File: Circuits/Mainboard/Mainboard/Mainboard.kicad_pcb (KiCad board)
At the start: 2 copper layers, 170.1 x 170.1 mm, 71 parts, among them IC1 LM74500QDDFRQ1, IC2 LM74500QDDFRQ1, IC3 2536030320001, IC4 SX1280IMLTRT, IC5 SKY66122-11, IC6 TS2596CM533_RNG, IC7 TPS563300DRLR, J1 XT60PW-M, J10 B5P-VH_LF__SN_, J11 B6B-PH-K-S, J12 B5P-VH_LF__SN_, J13 B6B-PH-K-S, J14 B5P-VH_LF__SN_, J15 SMA-J-P-H-RA-TH1, J16 B5P-VH_LF__SN_, J2 XT60PW-M, J22 Conn_01x04_Pin, J23 Conn_01x04_Pin, J25 Conn_01x06_Pin, J26 Conn_01x04_Pin, J27 Conn_01x04_Pin, J3 Conn_01x06_Pin, J5 B6B-PH-K-S, J6 B5P-VH_LF__SN_, J7 B6B-PH-K-S, J8 Conn_01x06_Pin, J9 Conn_01x04_Pin, Q1 PSMN6R7-40MLDX, Q2 PSMN6R7-40MLDX, U1 NUCLEOH723ZG

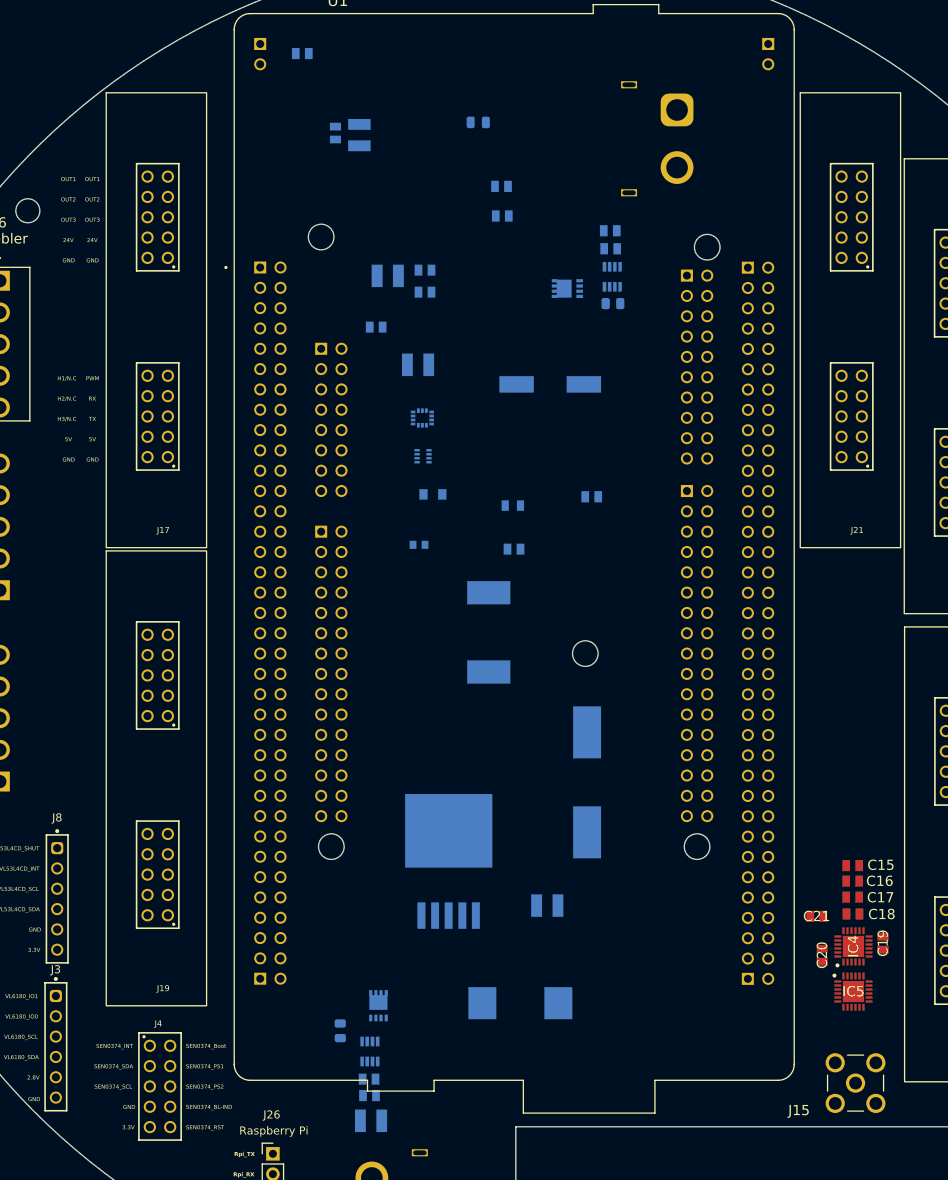
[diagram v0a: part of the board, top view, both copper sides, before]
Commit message: Removed components from the pcb to make it easier to work with
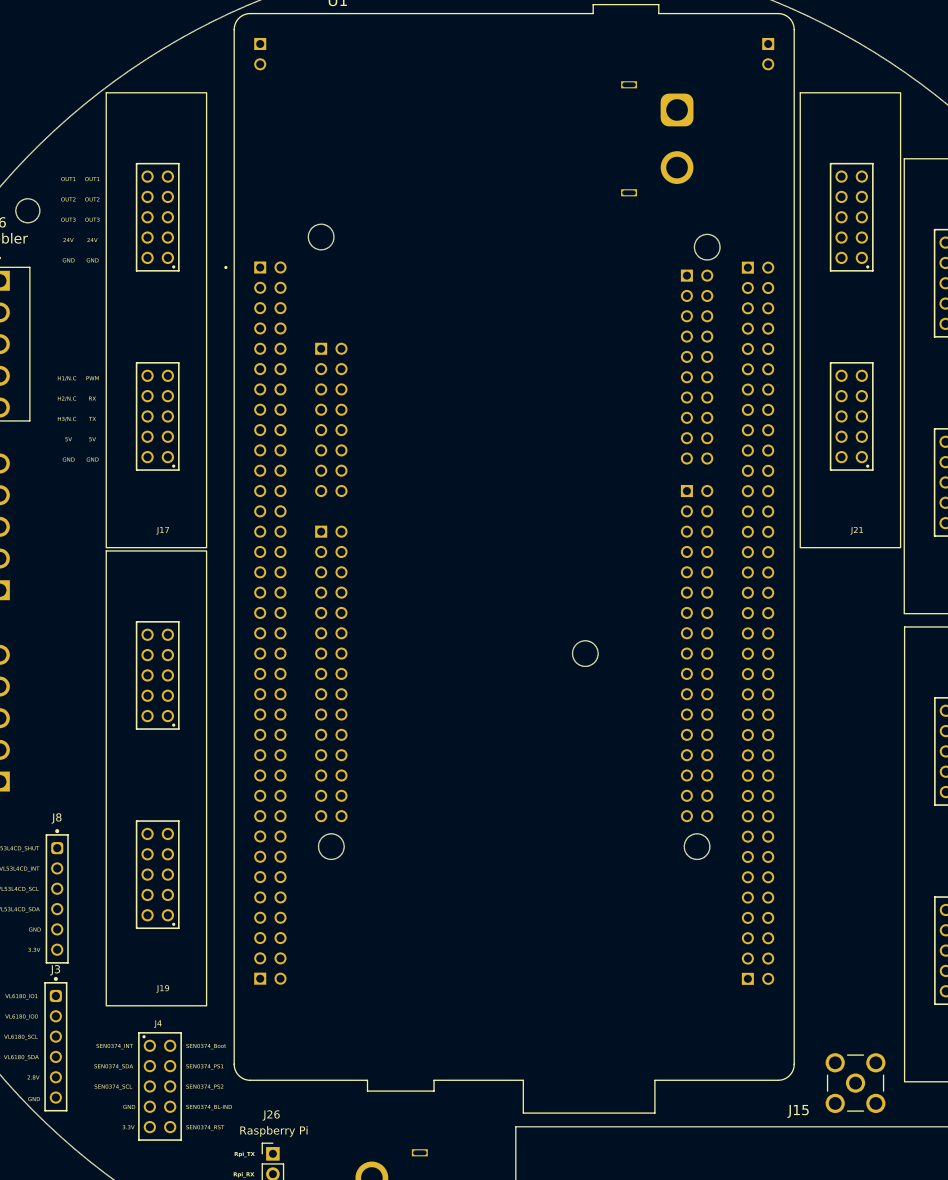
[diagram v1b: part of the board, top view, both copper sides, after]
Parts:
- removed C1, C12, C13, C14, C2, C23, C25, C26, C27, C3, C4, C6, C7: 0.1uF, 885012007063:CAPC2012X90N
- removed C10, C11, C24, C8, C9: 10uF, 885012209073:CAPC3225X280N
- removed C15, C17: 100nF, 885012007063:CAPC2012X90N
- removed C16, C18: 1nF, 885012007063:CAPC2012X90N
- removed C19: 1uF, 885012007063:CAPC2012X90N
- removed C20, C21: 10nF, 885012007063:CAPC2012X90N
- removed C22: 470uF, Altium_WCAP-ASLL (rev24b):WCAP-ASLL_D16H17
- removed C28: 47uF, Altium_WCAP-CSGP (rev24b):WCAP-CSGP_0805_L2W1.25H1.25
- removed C5: 220uF, 865080657018:CAPAE1030X1050N
- removed C8: 0.1uF, Capacitor_SMD:C_0805_2012Metric
- removed IC1, IC2: LM74500QDDFRQ1, LM74500QDDFRQ1:SOT65P280X110-8N
- removed IC3: 2536030320001, WSEN-ISDS:2536030320001
- removed IC4: SX1280IMLTRT, SX1280IMLTRT:QFN50P400X400X100-25N-D
- removed IC5: SKY66122-11, SKY66122-11:QFN50P400X400X100-25N-D
- removed IC6: TS2596CM533_RNG, TS2596CM533_RNG:TS2596CM550RNG
- removed IC7: TPS563300DRLR, TPS563300DRLR:TPS62932DRLR
- removed L1: 8.2uH, WE-HCC (rev24a):WE-HCC_1210
- removed L2: AMRM00101040470MA1, AMRM00101040470MA1:AMRM00101040470MA1
- removed Q1, Q2: PSMN6R7-40MLDX, PSMN6R740MLDX:PSMN6R740MLDX
- removed R1, R2: 10, Resistor_SMD:R_0805_2012Metric
- removed R3: 52.3kOhm, CRCW060352K3FKEA:RESC1608X50N
- removed R4: 10kOhm, Altium_WRIS-RSKS (rev23a):WRIS-RSKS_0805_Wave

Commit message: STP to pointer
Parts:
- added C1: 0.1uF, 885012007063:CAPC2012X90N, F.Cu at (62.9, 80.8)
- added C10: 0.1uF, 885012007063:CAPC2012X90N, F.Cu at (64.7, 49.6)
- added C10: 10uF, 885012209073:CAPC3225X280N, F.Cu at (49.6, 109.8)
- added C11: 10uF, 885012209073:CAPC3225X280N, F.Cu at (49.6, 114.0)
- added C12: 0.1uF, 885012007063:CAPC2012X90N, F.Cu at (66.8, 83.6)
- added C13: 10uF, 885012209073:CAPC3225X280N, F.Cu at (79.5, 41.4)
- added C14: 0.1uF, 885012007063:CAPC2012X90N, F.Cu at (66.8, 86.3)
- added C15: 100nF, 885012007063:CAPC2012X90N, F.Cu at (66.8, 89.1)
- added C16: 1nF, 885012007063:CAPC2012X90N, F.Cu at (66.8, 91.8)
- added C17: 100nF, 885012007063:CAPC2012X90N, F.Cu at (70.7, 80.8)
- added C18: 1nF, 885012007063:CAPC2012X90N, F.Cu at (70.7, 83.6)
- added C19: 1uF, 885012007063:CAPC2012X90N, F.Cu at (70.7, 86.3)
- added C2: 0.1uF, 885012007063:CAPC2012X90N, F.Cu at (62.9, 83.6)
- added C20: 10nF, 885012007063:CAPC2012X90N, F.Cu at (70.7, 89.1)
- added C21: 10nF, 885012007063:CAPC2012X90N, F.Cu at (70.7, 91.8)
- added C22: 470uF, Altium_WCAP-ASLL (rev24b):WCAP-ASLL_D16H17, F.Cu at (56.9, 70.2)
- added C22: 0.1uF, 885012007063:CAPC2012X90N, F.Cu at (64.7, 52.3)
- added C23: 47uF, Altium_WCAP-CSGP (rev24b):WCAP-CSGP_0805_L2W1.25H1.25, F.Cu at (78.2, 49.4)
- added C23: 0.1uF, 885012007063:CAPC2012X90N, F.Cu at (74.7, 80.8)
- added C24: 10uF, 885012209073:CAPC3225X280N, F.Cu at (49.6, 118.2)
- added C25: 0.1uF, 885012007063:CAPC2012X90N, F.Cu at (74.7, 83.6)
- added C26: 0.1uF, 885012007063:CAPC2012X90N, F.Cu at (74.7, 86.3)
- added C27: 0.1uF, 885012007063:CAPC2012X90N, F.Cu at (74.7, 89.1)
- added C28: 47uF, Altium_WCAP-CSGP (rev24b):WCAP-CSGP_0805_L2W1.25H1.25, F.Cu at (92.5, 71.1)
- added C29: 100nF, 885012007063:CAPC2012X90N, F.Cu at (74.7, 91.8)
- added C3: 0.1uF, 885012007063:CAPC2012X90N, F.Cu at (62.9, 86.3)
- added C30: 1nF, 885012007063:CAPC2012X90N, F.Cu at (78.6, 80.8)
- added C31: 100nF, 885012007063:CAPC2012X90N, F.Cu at (78.6, 83.6)
- added C32: 1nF, 885012007063:CAPC2012X90N, F.Cu at (78.6, 86.3)
- added C33: 100nF, 885012007063:CAPC2012X90N, F.Cu at (78.6, 89.1)
- added C34: 1nF, 885012007063:CAPC2012X90N, F.Cu at (78.6, 91.8)
- added C35: 0p8, Capacitor_SMD:C_0603_1608Metric, F.Cu at (54.3, 100.7)
- added C36: 1p5, Capacitor_SMD:C_0603_1608Metric, F.Cu at (54.3, 103.2)
- added C37: NA, Capacitor_SMD:C_0603_1608Metric, F.Cu at (54.3, 105.7)
- added C38: 0p5, Capacitor_SMD:C_0603_1608Metric, F.Cu at (54.3, 108.2)
- added C39: 100p, Capacitor_SMD:C_0603_1608Metric, F.Cu at (54.3, 110.7)
- added C4: 0.1uF, 885012007063:CAPC2012X90N, F.Cu at (62.9, 89.1)
- added C40: 47p, Capacitor_SMD:C_0603_1608Metric, F.Cu at (54.3, 113.2)
- added C41: 0p6, Capacitor_SMD:C_0603_1608Metric, F.Cu at (54.3, 115.7)
- added C42: NA, Capacitor_SMD:C_0603_1608Metric, F.Cu at (54.3, 118.2)
- added C43: 4.7uF, 885012209073:CAPC3225X280N, F.Cu at (79.5, 45.5)
- added C44: 0.1uF, 885012007063:CAPC2012X90N, F.Cu at (64.7, 55.1)
- added C5: 220uF, 865080657018:CAPAE1030X1050N, F.Cu at (84.4, 99.5)
- added C6: 0.1uF, 885012007063:CAPC2012X90N, F.Cu at (62.9, 91.8)
- added C7: 0.1uF, 885012007063:CAPC2012X90N, F.Cu at (66.8, 80.8)
- added C7: 10uF, 885012209073:CAPC3225X280N, F.Cu at (79.5, 37.2)
- added C8: 10uF, 885012209073:CAPC3225X280N, F.Cu at (49.6, 101.5)
- added C9: 10uF, 885012209073:CAPC3225X280N, F.Cu at (49.6, 105.7)
- added IC1: LM74500QDDFRQ1, LM74500QDDFRQ1:SOT65P280X110-8N, F.Cu at (93.2, 63.2)
- added IC2: LM74500QDDFRQ1, LM74500QDDFRQ1:SOT65P280X110-8N, F.Cu at (93.2, 67.7)
- added IC3: 2536030320001, WSEN-ISDS:2536030320001, F.Cu at (83.6, 89.2)
- added IC4: SX1280IMLTRT, SX1280IMLTRT:QFN50P400X400X100-25N-D, F.Cu at (94.0, 108.9)
- added IC5: SKY66122-11, SKY66122-11:QFN50P400X400X100-25N-D, F.Cu at (94.0, 115.2)
- added IC6: TS2596CM533_RNG, TS2596CM533_RNG:TS2596CM550RNG, F.Cu at (53.9, 90.9)
- added IC6: TPS563300DRLR, TPS563300DRLR:TPS62932DRLR, F.Cu at (69.3, 50.8)
- added IC7: TPS563300DRLR, TPS563300DRLR:TPS62932DRLR, F.Cu at (89.3, 89.0)
- added L1: 8.2uH, WE-HCC (rev24a):WE-HCC_1210, F.Cu at (83.9, 112.2)
- added L2: AMRM00101040470MA1, AMRM00101040470MA1:AMRM00101040470MA1, F.Cu at (69.0, 100.5)
- added L2: 5.6uH, Power Inductors - SMD WE-PD 5.6uH 6A:7447714220, F.Cu at (69.8, 41.7)
- added P1: 66200621122, WR-MPC3 3.00 mm Male Header Dual Row Vertical:66200621122, F.Cu at (158.6, 61.8)
- added Q1: PSMN6R7-40MLDX, PSMN6R740MLDX:PSMN6R740MLDX, F.Cu at (83.8, 82.8)
- added Q2: PSMN6R7-40MLDX, PSMN6R740MLDX:PSMN6R740MLDX, F.Cu at (90.2, 82.8)
- added R1: 10, Resistor_SMD:R_0805_2012Metric, F.Cu at (58.5, 100.9)
- added R2: 10, Resistor_SMD:R_0805_2012Metric, F.Cu at (58.5, 103.8)
- added R3: 52.3kOhm, CRCW060352K3FKEA:RESC1608X50N, F.Cu at (93.8, 90.0)
- added R4: 10kOhm, Altium_WRIS-RSKS (rev23a):WRIS-RSKS_0805_Wave, F.Cu at (94.1, 87.6)
- added R5: 3n, Resistor_SMD:R_0805_2012Metric, F.Cu at (58.5, 106.8)
- added R6: 2n7, Resistor_SMD:R_0805_2012Metric, F.Cu at (58.5, 109.7)
- added R7: 3n9, Resistor_SMD:R_0805_2012Metric, F.Cu at (58.5, 112.7)
- added R8: 30.9kOhm, Resistor_SMD:R_0805_2012Metric, F.Cu at (68.8, 54.9)
- added R9: 10kOhm, Altium_WRIS-RSKS (rev23a):WRIS-RSKS_0805_Wave, F.Cu at (74.1, 49.4)
- added U2: ADP121-AUJZ28R7, ADP121-AUJZ28R7:UJ-5_ADI, F.Cu at (109.0, 58.7)
- J17: value ~ -> Conn_01x04_Pin; footprint 61301021821:ESC_Adapter_socket -> Connector_PinHeader_2.54mm:PinHeader_1x04_P2.54mm_Vertical; moved to B.Cu
- J18, J19, J20, J21: footprint 61301021821:ESC_Adapter_socket -> B-G431B-ESC1:ESC_Adapter_socket
- J22: value Conn_01x04_Pin -> ~; footprint Connector_PinHeader_2.54mm:PinHeader_1x04_P2.54mm_Vertical -> B-G431B-ESC1:ESC_Adapter_socket; moved to F.Cu
- moved J1 120.1 mm to (191.1, 182.5), turned to 0 degrees
- moved J4 105.3 mm to (244.8, 162.3)
- moved J26 101.0 mm to (241.9, 140.6)
- moved J18 41.3 mm to (227.7, 78.1)
- moved J22 37.8 mm to (141.6, 78.5), turned to 0 degrees
- moved J20 36.9 mm to (227.7, 141.2)
- moved J17 31.3 mm to (111.3, 101.4), turned to 180 degrees
- moved J21 26.9 mm to (240.2, 84.6)
- moved J19 24.6 mm to (141.6, 141.4)
- moved J2 22.3 mm to (172.0, 182.1), turned to 0 degrees
- moved U1 19.1 mm to (185.0, 137.1)
- moved J15 14.4 mm to (239.9, 175.8)
- moved J23 0.31 mm to (111.3, 148.1)
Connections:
- J11 pad 2: /5V -> 5V
- J13 pad 2: /5V -> 5V
- J15 pad 1: unconnected-(J15-Pad1) -> Net-(C42-Pad2)
- J15 pad 2: unconnected-(J15-Pad2) -> GND
- J15 pad 3: unconnected-(J15-Pad3) -> GND
- J15 pad 4: unconnected-(J15-Pad4) -> GND
- J15 pad 5: unconnected-(J15-Pad5) -> GND
- J17 pad 1: GND -> 5V
- J17 pad 2: GND -> /M1_Encoder_A
- J17 pad 3: /5V -> /M1_Encoder_B
- J17 pad 4: /5V -> GND
- J18 pad 1: GND -> /M2_OUT1
- J18 pad 10: /M2_H1 -> /M2_OUT3
- J18 pad 11: GND -> /M2_OUT3
- J18 pad 12: GND -> /M2_OUT3
- J18 pad 15: /M2_OUT3 -> 24V
- J18 pad 16: /M2_OUT3 -> 24V
- J18 pad 17: /M2_OUT2 -> GND
- J18 pad 18: /M2_OUT2 -> GND
- J18 pad 19: /M2_OUT1 -> GND
- J18 pad 2: GND -> /M2_OUT1
- J18 pad 20: /M2_OUT1 -> GND
- J18 pad 3: /5V -> /M2_OUT1
- J18 pad 4: /5V -> /M2_OUT1
- J18 pad 5: /M2_TX -> /M2_OUT2
- J18 pad 6: /M2_H3 -> /M2_OUT2
- J18 pad 7: /M2_RX -> /M2_OUT2
- J18 pad 8: /M2_H2 -> /M2_OUT2
- J18 pad 9: /M2_PWM -> /M2_OUT3
- J19 pad 1: GND -> /M3_OUT1
- J19 pad 10: /M3_H1 -> /M3_OUT3
- J19 pad 11: GND -> /M3_OUT3
- J19 pad 12: GND -> /M3_OUT3
- J19 pad 15: /M3_OUT3 -> 24V
- J19 pad 16: /M3_OUT3 -> 24V
- J19 pad 17: /M3_OUT2 -> GND
- J19 pad 18: /M3_OUT2 -> GND
- J19 pad 19: /M3_OUT1 -> GND
- J19 pad 2: GND -> /M3_OUT1
- J19 pad 20: /M3_OUT1 -> GND
- J19 pad 3: /5V -> /M3_OUT1
- J19 pad 4: /5V -> /M3_OUT1
- J19 pad 5: /M3_TX -> /M3_OUT2
- J19 pad 6: /M3_H3 -> /M3_OUT2
- J19 pad 7: /M3_RX -> /M3_OUT2
- J19 pad 8: /M3_H2 -> /M3_OUT2
- J19 pad 9: /M3_PWM -> /M3_OUT3
- J20 pad 1: GND -> /M4_OUT1
- J20 pad 10: /M4_H1 -> /M4_OUT3
- J20 pad 11: GND -> /M4_OUT3
- J20 pad 12: GND -> /M4_OUT3
- J20 pad 15: /M4_OUT3 -> 24V
- J20 pad 16: /M4_OUT3 -> 24V
- J20 pad 17: /M4_OUT2 -> GND
- J20 pad 18: /M4_OUT2 -> GND
- J20 pad 19: /M4_OUT1 -> GND
- J20 pad 2: GND -> /M4_OUT1
- J20 pad 20: /M4_OUT1 -> GND
- J20 pad 3: /5V -> /M4_OUT1
- J20 pad 4: /5V -> /M4_OUT1
- J20 pad 5: /M4_TX -> /M4_OUT2
- J20 pad 6: /M4_H3 -> /M4_OUT2
- J20 pad 7: /M4_RX -> /M4_OUT2
- J20 pad 8: /M4_H2 -> /M4_OUT2
- J20 pad 9: /M4_PWM -> /M4_OUT3
- J21 pad 1: GND -> /M5_OUT1
- J21 pad 10: unconnected-(J21-L10-Pad10) -> /M5_OUT3
- J21 pad 11: GND -> /M5_OUT3
- J21 pad 12: GND -> /M5_OUT3
- J21 pad 15: /M5_OUT3 -> 24V
- J21 pad 16: /M5_OUT3 -> 24V
- J21 pad 17: /M5_OUT2 -> GND
- J21 pad 18: /M5_OUT2 -> GND
- J21 pad 19: /M5_OUT1 -> GND
- J21 pad 2: GND -> /M5_OUT1
- J21 pad 20: /M5_OUT1 -> GND
- J21 pad 3: /5V -> /M5_OUT1
- J21 pad 4: /5V -> /M5_OUT1
- J21 pad 5: /M5_TX -> /M5_OUT2
- J21 pad 6: unconnected-(J21-L6-Pad6) -> /M5_OUT2
- J21 pad 7: /M5_RX -> /M5_OUT2
- J21 pad 8: unconnected-(J21-L8-Pad8) -> /M5_OUT2
- J21 pad 9: /M5_PWM -> /M5_OUT3
- J22 pad 1: /5V -> /M1_OUT1
- J22 pad 2: /M1_Encoder_A -> /M1_OUT1
- J22 pad 3: /M1_Encoder_B -> /M1_OUT1
- J22 pad 4: GND -> /M1_OUT1
- J23 pad 1: /5V -> 5V
- J26 pad 3: /5V -> 5V
- J27 pad 1: /5V -> 5V
- J3 pad 5: /2.8V -> 2.8V
- J5 pad 2: /5V -> 5V
- J5 pad 3: /M1_H3 -> /M1_H1
- J7 pad 2: /5V -> 5V
- J9 pad 1: /5V -> 5V
- U1 pad CN11_16: Net-(U1A-3V3) -> 3.3V
- U1 pad CN11_35: unconnected-(U1A-PC2-PadCN11_35) -> RF_MISO
- U1 pad CN11_37: unconnected-(U1A-PC3-PadCN11_37) -> RF_MOSI
- U1 pad CN11_42: unconnected-(U1A-PG2-PadCN11_42) -> /SEN0374_PS2
- U1 pad CN11_44: unconnected-(U1A-PG3-PadCN11_44) -> /SEN0374_BL-IND
- U1 pad CN11_52: unconnected-(U1A-PF2-PadCN11_52) -> /VL53L4CD_SHUT
- U1 pad CN12_2: unconnected-(U1B-PC8-PadCN12_2) -> /VL6180_IO0
- U1 pad CN12_25: unconnected-(U1B-PB10-PadCN12_25) -> RF_SCK
- U1 pad CN12_41: unconnected-(U1B-PD13-PadCN12_41) -> /SEN0374_INT
- U1 pad CN12_46: unconnected-(U1B-PD14-PadCN12_46) -> /SEN0374_Boot
- U1 pad CN12_48: unconnected-(U1B-PD15-PadCN12_48) -> /SEN0374_PS1
- U1 pad CN12_53: unconnected-(U1B-PE15-PadCN12_53) -> RF_CS
- U1 pad CN12_58: unconnected-(U1B-PF3-PadCN12_58) -> /VL53L4CD_INT
- U1 pad CN12_66: unconnected-(U1B-PG8-PadCN12_66) -> /VL6180_IO1
- U1 pad CN12_68: unconnected-(U1B-PG5-PadCN12_68) -> /ADPS-9960_VL
- U1 pad CN12_69: unconnected-(U1B-PG4-PadCN12_69) -> /SEN0374_RST
- U1 pad CN12_70: unconnected-(U1B-PG6-PadCN12_70) -> /ADPS-9960_INT
- U1 pad CN8_12: GND -> unconnected-(U1C-D48/SDMMC_CMD-PadCN8_12)
- U1 pad CN8_14: GND -> unconnected-(U1C-D49/IO-PadCN8_14)
- U1 pad CN8_8: 3.3V -> unconnected-(U1C-D46/SDMMC_D3-PadCN8_8)
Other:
- board size 170.1 x 170.1 mm -> 170 x 170 mm
- board text added: "RX/N.C"
- board text removed: "RX"

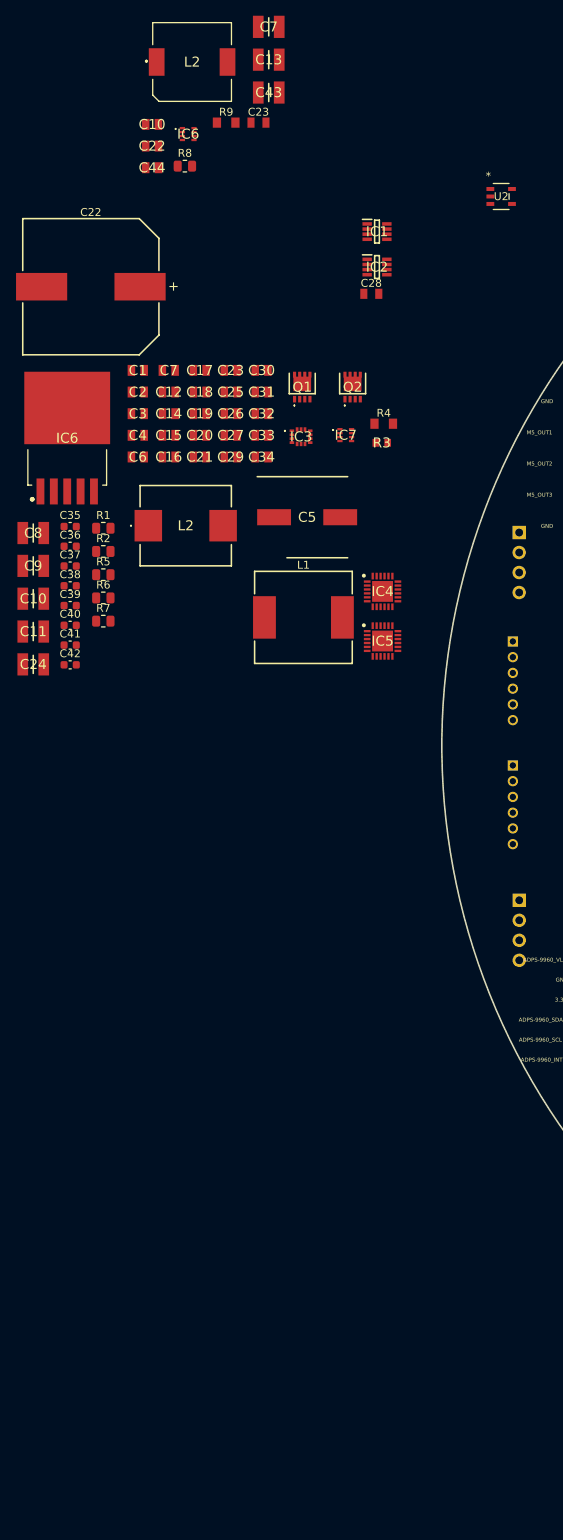
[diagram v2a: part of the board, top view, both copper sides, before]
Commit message: Added updated pin configuration to stm32
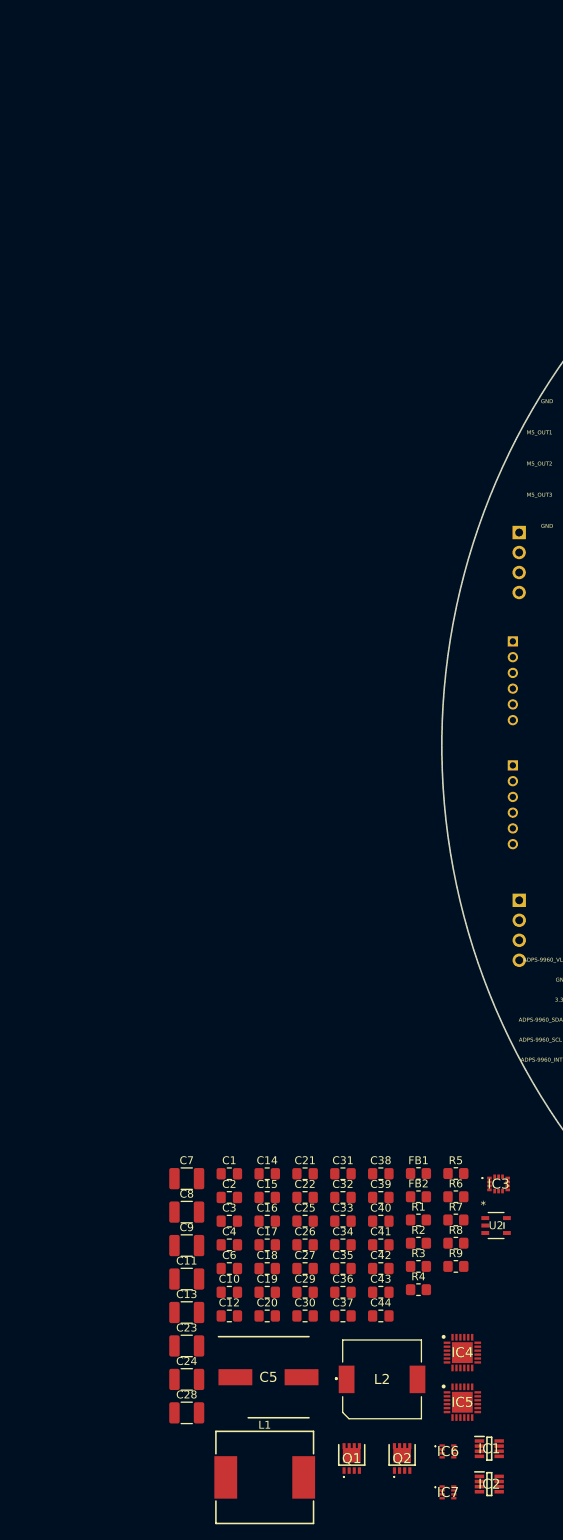
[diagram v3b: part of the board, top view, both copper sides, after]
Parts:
- removed the C10 at (64.7, 49.6)
- removed the C10 at (49.6, 109.8)
- removed the C22 at (56.9, 70.2)
- removed the C22 at (64.7, 52.3)
- removed the C23 at (78.2, 49.4)
- removed the C23 at (74.7, 80.8)
- removed the C7 at (66.8, 80.8)
- removed the C7 at (79.5, 37.2)
- removed the IC6 at (53.9, 90.9)
- removed the IC6 at (69.3, 50.8)
- removed the L2 at (69.0, 100.5)
- removed the L2 at (69.8, 41.7)
- added C10: 0.1uF, Capacitor_SMD:C_0805_2012Metric_Pad1.18x1.45mm_HandSolder, F.Cu at (74.5, 197.9)
- added C22: 0.1uF, Capacitor_SMD:C_0805_2012Metric_Pad1.18x1.45mm_HandSolder, F.Cu at (84.1, 185.9)
- added C23: 47uF, Capacitor_SMD:C_1210_3225Metric_Pad1.33x2.70mm_HandSolder, F.Cu at (69.1, 204.7)
- added C7: 10uF, Capacitor_SMD:C_1210_3225Metric_Pad1.33x2.70mm_HandSolder, F.Cu at (69.1, 183.5)
- added FB1: 120R, Resistor_SMD:R_0805_2012Metric_Pad1.20x1.40mm_HandSolder, F.Cu at (98.5, 182.8)
- added FB2: 120R, Resistor_SMD:R_0805_2012Metric_Pad1.20x1.40mm_HandSolder, F.Cu at (98.5, 185.8)
- added IC6: TPS563300DRLR, TPS563300DRLR:TPS62932DRLR, F.Cu at (102.3, 218.1)
- added L2: 5.6uH, Power Inductors - SMD WE-PD 5.6uH 6A:7447714220, F.Cu at (93.9, 209.0)
- C1, C12, C14, C15, C16, C17, C18, C19, C2, C20, C21, C25, C26, C27, C29, C3, C30, C31, C32, C33, C34, C4, C44, C6: footprint 885012007063:CAPC2012X90N -> Capacitor_SMD:C_0805_2012Metric_Pad1.18x1.45mm_HandSolder
- C11, C13, C24, C8, C9: footprint 885012209073:CAPC3225X280N -> Capacitor_SMD:C_1210_3225Metric_Pad1.33x2.70mm_HandSolder
- C28: footprint Altium_WCAP-CSGP (rev24b):WCAP-CSGP_0805_L2W1.25H1.25 -> Capacitor_SMD:C_1210_3225Metric_Pad1.33x2.70mm_HandSolder
- C35, C36, C37, C38, C39, C40, C41, C42: footprint Capacitor_SMD:C_0603_1608Metric -> Capacitor_SMD:C_0805_2012Metric_Pad1.18x1.45mm_HandSolder
- C43: footprint 885012209073:CAPC3225X280N -> Capacitor_SMD:C_0805_2012Metric_Pad1.18x1.45mm_HandSolder
- C5: footprint 865080657018:CAPAE1030X1050N -> WCAP-ASLI Aluminum Electrolytic Capacitors:CAPAE1030X1050N
- L1: footprint WE-HCC (rev24a):WE-HCC_1210 -> WE-HCC SMT High Current Cube Inductor:WE-HCC_1210
- R1, R2, R5, R6, R7, R8: footprint Resistor_SMD:R_0805_2012Metric -> Resistor_SMD:R_0805_2012Metric_Pad1.20x1.40mm_HandSolder
- R3: footprint CRCW060352K3FKEA:RESC1608X50N -> Resistor_SMD:R_0805_2012Metric_Pad1.20x1.40mm_HandSolder
- R4, R9: footprint Altium_WRIS-RSKS (rev23a):WRIS-RSKS_0805_Wave -> Resistor_SMD:R_0805_2012Metric_Pad1.20x1.40mm_HandSolder
- moved C13 159.5 mm to (69.1, 200.5)
- moved IC1 155.2 mm to (107.5, 217.8)
- moved IC2 155.2 mm to (107.5, 222.3)
- moved C43 153.0 mm to (93.7, 197.9)
- moved C44 148.7 mm to (93.7, 200.9)
- moved R9 148.2 mm to (103.3, 194.6)
- moved C28 144.0 mm to (69.1, 213.2)
- moved R8 141.1 mm to (103.3, 191.7)
- moved Q1 136.2 mm to (90.0, 218.9)
- moved Q2 136.2 mm to (96.4, 218.9)
- moved IC7 134.9 mm to (102.3, 223.3)
- moved U2 130.7 mm to (108.4, 189.4)
- moved C30 120.2 mm to (84.1, 200.9)
- moved C12 117.6 mm to (74.5, 200.9)
- moved C20 112.2 mm to (79.3, 200.9)
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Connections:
- C28 pad 1: GND -> 5V
- C28 pad 2: 5V -> GND

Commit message: Updated pin connections for the mainboard controller
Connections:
- U1 pad CN11_1: unconnected-(U1A-PC10-PadCN11_1) -> /M5_TX
- U1 pad CN11_17: unconnected-(U1A-PA15-PadCN11_17) -> /M1_Encoder_A
- U1 pad CN11_21: /SEN0374_SDA -> /M3_Encoder_B
- U1 pad CN11_28: /M5_TX -> /M1_PWM
- U1 pad CN11_30: unconnected-(U1A-PA1-PadCN11_30) -> /M1_Encoder_B
- U1 pad CN11_50: unconnected-(U1A-PE5-PadCN11_50) -> /M2_PWM
- U1 pad CN11_63: unconnected-(U1A-PG9-PadCN11_63) -> /M3_RX
- U1 pad CN11_9: unconnected-(U1A-PF6-PadCN11_9) -> /M3_PWM
- U1 pad CN12_19: /M3_RX -> /M4_Encoder_B
- U1 pad CN12_27: unconnected-(U1B-PB4-PadCN12_27) -> /M2_Encoder_A
- U1 pad CN12_28: unconnected-(U1B-PB14-PadCN12_28) -> /M5_PWM
- U1 pad CN12_29: unconnected-(U1B-PB5-PadCN12_29) -> /M2_Encoder_B
- U1 pad CN12_4: /M3_TX -> /M4_Encoder_A
- U1 pad CN12_43: unconnected-(U1B-PD12-PadCN12_43) -> /M3_Encoder_A
- U1 pad CN12_5: unconnected-(U1B-PB9-PadCN12_5) -> /SEN0374_SDA
- U1 pad CN12_61: unconnected-(U1B-PG14-PadCN12_61) -> /M3_TX
- U1 pad CN12_62: unconnected-(U1B-PF11-PadCN12_62) -> /M4_PWM

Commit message: Added stm32cubemx project
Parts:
- added J24: Conn_01x06_Pin, Socket_header_6_pins_single_straight:61300611821, F.Cu at (133.5, 162.0)
- C5, L1: moved to B.Cu
- moved C8 132.0 mm to (199.9, 170.1), turned to 90 degrees
- moved J26 130.6 mm to (121.7, 89.5)
- moved J16 129.4 mm to (250.7, 98.4), turned to 90 degrees
- moved L1 127.7 mm to (173.4, 135.5), turned to 180 degrees
- moved C28 127.1 mm to (175.7, 144.0)
- moved C1 122.1 mm to (195.9, 170.1), turned to 90 degrees
- moved C3 119.7 mm to (192.8, 170.1), turned to 90 degrees
- moved C5 115.9 mm to (181.2, 153.2), turned to 90 degrees
- moved C11 115.4 mm to (181.5, 170.1), turned to 90 degrees
- moved Q1 114.7 mm to (190.1, 163.0), turned to -90 degrees
- moved C9 108.7 mm to (171.9, 156.8), turned to -90 degrees
- moved C6 108.3 mm to (175.9, 157.0), turned to -90 degrees
- moved C2 104.3 mm to (177.6, 170.1), turned to 90 degrees
- moved C27 102.8 mm to (175.1, 147.1), turned to 180 degrees
- moved C4 102.4 mm to (174.5, 170.1), turned to 90 degrees
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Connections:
- J12 pad 2: /M3_OUT3 -> /M3_OUT1
- U1 pad CN11_40: unconnected-(U1A-PD3-PadCN11_40) -> RF_SCK
- U1 pad CN11_51: /VL53L4CD_SCL -> /VL53L4CD2_SCL
- U1 pad CN11_53: /VL53L4CD_SDA -> /VL53L4CD2_SDA
- U1 pad CN12_18: unconnected-(U1B-PB11-PadCN12_18) -> /VL53L4CD_SDA
- U1 pad CN12_25: RF_SCK -> /VL53L4CD_SCL
- U1 pad CN12_36: unconnected-(U1B-PF5-PadCN12_36) -> /VL53L4CD2_SHUT
- U1 pad CN12_38: unconnected-(U1B-PF4-PadCN12_38) -> /VL53L4CD2_INT
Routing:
- net 5V: track 0.00 -> 112.9 mm
- net /M1_OUT1: track 0.00 -> 96.5 mm
- net /M1_OUT2: track 0.00 -> 79.1 mm
- net /M1_H3: track 0.00 -> 62.2 mm
- net /M1_OUT3: track 0.00 -> 59.4 mm
- net /M1_H2: track 0.00 -> 56.4 mm
- net /M1_H1: track 0.00 -> 53.4 mm
- net /24V_1: track 0.00 -> 36.5 mm
- net /24V_2: track 0.00 -> 33.5 mm
- net 24V: track 0.00 -> 21.6 mm, vias 0 -> 6
- net /M3_OUT3: track 0.00 -> 20.5 mm
- net Net-(IC1-GATE): track 0.00 -> 4.18 mm
- net Net-(IC2-GATE): track 0.00 -> 4.08 mm
- net Net-(Q2-G): track 0.00 -> 3.47 mm
- net Net-(Q1-G): track 0.00 -> 3.45 mm
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- added copper zone on B.Cu, net 24V
- added copper zone on F.Cu, net 24V
- added copper zone on B.Cu, net GND
